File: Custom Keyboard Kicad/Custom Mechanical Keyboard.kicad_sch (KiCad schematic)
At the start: 288 parts, among them J1 USB_C_Receptacle_USB2.0_16P, J2 Conn_01x04, J3 Conn_01x05, J4 Conn_01x06, J5 Conn_01x07, J6 Conn_01x20_Socket, J7 Conn_01x20_Socket, SW1 SW_SPST, SW10 SW_SPST, SW11 SW_SPST, SW12 SW_SPST, SW13 SW_SPST, SW14 SW_SPST, SW15 SW_SPST, SW16 SW_SPST, SW17 SW_SPST, SW18 SW_SPST, SW19 SW_SPST, SW2 SW_SPST, SW20 SW_SPST, SW21 SW_SPST, SW22 SW_SPST, SW23 SW_SPST, SW24 SW_SPST, SW25 SW_SPST, SW26 SW_SPST, SW27 SW_SPST, SW28 SW_SPST, SW29 SW_SPST, SW3 SW_SPST, SW30 SW_SPST, SW31 SW_SPST, SW32 SW_SPST, SW33 SW_SPST, SW34 SW_SPST, SW35 SW_SPST, SW36 SW_SPST, SW37 SW_SPST, SW38 SW_SPST, SW39 SW_SPST, SW4 SW_SPST, SW40 SW_SPST, SW41 SW_SPST, SW42 SW_SPST, SW43 SW_SPST, SW44 SW_SPST, SW45 SW_SPST, SW46 SW_SPST, SW47 SW_SPST, SW48 SW_SPST, SW49 SW_SPST, SW5 SW_SPST, SW50 SW_SPST, SW51 SW_SPST, SW52 SW_SPST, SW53 SW_SPST, SW54 SW_SPST, SW55 SW_SPST, SW56 SW_SPST, SW57 SW_SPST, SW58 SW_SPST, SW59 SW_SPST, SW6 SW_SPST, SW60 SW_SPST, SW61 SW_SPST, SW62 SW_SPST, SW63 SW_SPST, SW64 SW_SPST, SW65 SW_SPST, SW66 SW_SPST, SW67 SW_SPST, SW68 SW_SPST, SW69 SW_SPST, SW7 SW_SPST, SW70 SW_SPST, SW71 SW_SPST, SW72 SW_SPST, SW73 SW_SPST, SW74 SW_SPST, SW75 SW_SPST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

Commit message: Commit after exports
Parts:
- J6, J7: MFG Part # (none) -> FPC-05F-20PH20; Manufacturer (none) -> Xunpu; Type (none) -> SMD
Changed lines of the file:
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@@
 			)
 		)
+		(property "MFG Part #" "FPC-05F-20PH20"
+			(at 488.95 92.71 0)
+			(effects
+				(font
+					(size 1.27 1.27)
+				)
+				(hide yes)
+			)
+		)
+		(property "Manufacturer" "Xunpu"
+			(at 488.95 92.71 0)
+			(effects
+				(font
+					(size 1.27 1.27)
+				)
+				(hide yes)
+			)
+		)
+		(property "Type" "SMD"
+			(at 488.95 92.71 0)
+			(effects
+				(font
+					(size 1.27 1.27)
+				)
+				(hide yes)
+			)
+		)
 		(pin "7"
 		)
@@
 			(at 509.27 92.71 0)
 			(effects
+				(font
+					(size 1.27 1.27)
+				)
+				(hide yes)
+			)
+		)
+		(property "MFG Part #" "FPC-05F-20PH20"
+			(at 509.27 92.71 0)
+			(effects
+				(font
+					(size 1.27 1.27)
+				)
+				(hide yes)
+			)
+		)
+		(property "Manufacturer" "Xunpu"
+			(at 509.27 92.71 0)
+			(effects
+				(font
+					(size 1.27 1.27)
+				)
+				(hide yes)
+			)
+		)
+		(property "Type" "SMD"
+			(at 509.27 92.71 0)
+			(effects

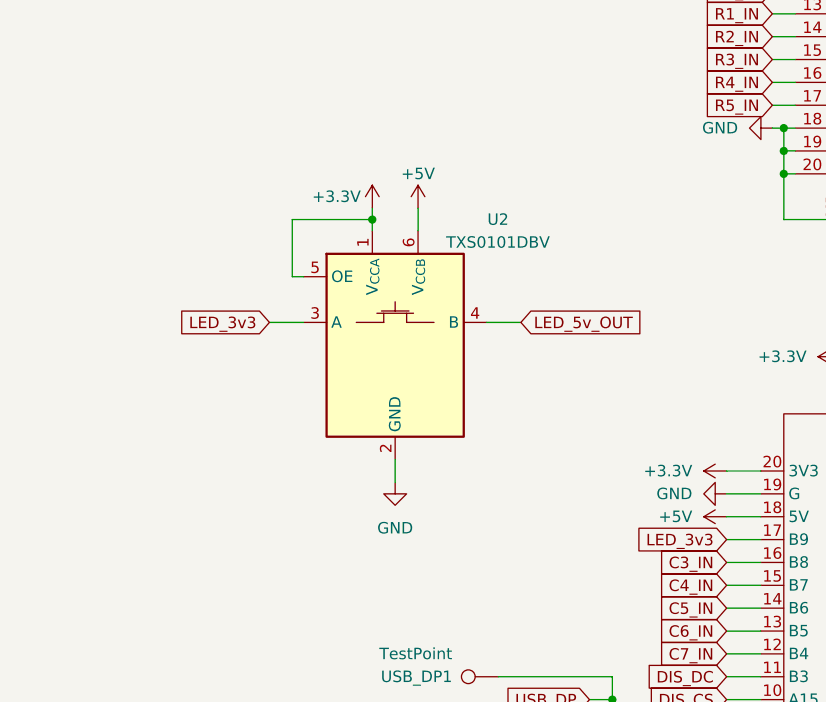
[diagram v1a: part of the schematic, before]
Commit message: Feat: Changed level shifter from TXS0101DBV to SN74LVC1T45DBV, footprint and wiring not changed.
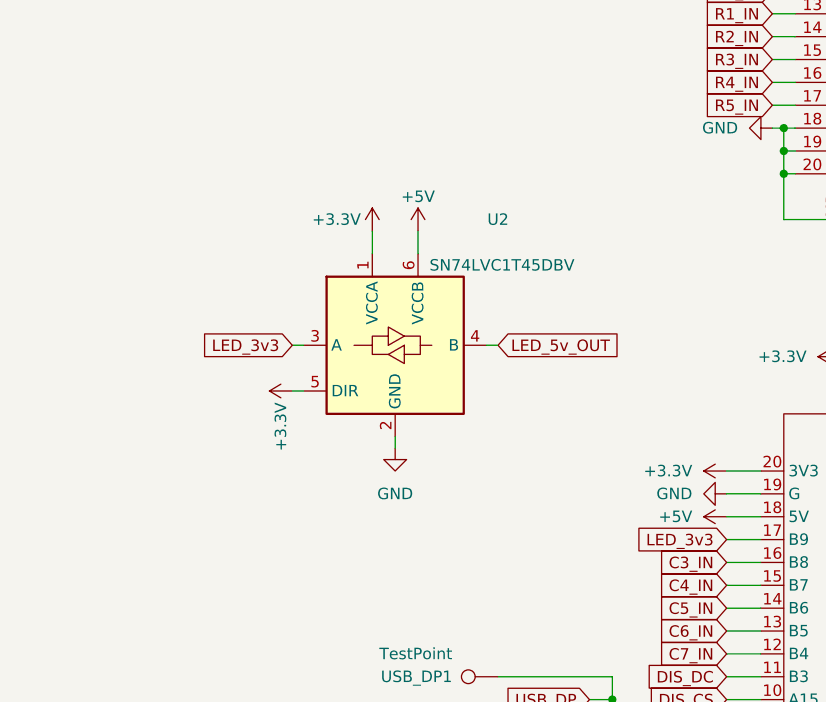
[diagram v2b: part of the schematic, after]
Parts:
- U2: value TXS0101DBV -> SN74LVC1T45DBV; symbol Logic_LevelTranslator:TXS0101DBV -> Logic_LevelTranslator:SN74LVC1T45DBV; MFG Part # TXS0101DBV -> SN74LVC1T45DBV\
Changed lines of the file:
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@@
 	)
 	(junction
-		(at 436.88 123.19)
-		(diameter 0)
-		(color 0 0 0 0)
-	)
-	(junction
 		(at 266.7 99.06)
 		(diameter 0)
@@
 	(wire
 		(pts
-			(xy 436.88 121.92) (xy 436.88 123.19)
-		)
-		(stroke
-			(width 0)
-			(type default)
-		)
-	)
-	(wire
-		(pts
 			(xy 374.65 332.74) (xy 374.65 330.2)
 		)
@@
 	(wire
 		(pts
-			(xy 441.96 121.92) (xy 441.96 124.46)
+			(xy 441.96 124.46) (xy 441.96 127)
 		)
 		(stroke
@@
 	(wire
 		(pts
-			(xy 144.78 54.61) (xy 144.78 55.88)
+			(xy 436.88 124.46) (xy 436.88 127)
 		)
 		(stroke
@@
 	(wire
 		(pts
-			(xy 63.5 142.24) (xy 83.82 142.24)
+			(xy 144.78 54.61) (xy 144.78 55.88)
 		)
 		(stroke
@@
 	(wire
 		(pts
-			(xy 340.36 36.83) (xy 340.36 45.72)
+			(xy 63.5 142.24) (xy 83.82 142.24)
 		)
 		(stroke
@@
 	(wire
 		(pts
-			(xy 320.04 67.31) (xy 318.77 67.31)
+			(xy 340.36 36.83) (xy 340.36 45.72)
 		)
 		(stroke
@@
 	(wire
 		(pts
-			(xy 171.45 210.82) (xy 191.77 210.82)
+			(xy 320.04 67.31) (xy 318.77 67.31)
 		)
 		(stroke
@@
 	(wire
 		(pts
-			(xy 427.99 123.19) (xy 436.88 123.19)
+			(xy 171.45 210.82) (xy 191.77 210.82)
 		)
 		(stroke
@@
 	(wire
 		(pts
-			(xy 425.45 134.62) (xy 429.26 134.62)
+			(xy 427.99 137.16) (xy 429.26 137.16)
 		)
 		(stroke
@@
 	(wire
 		(pts
-			(xy 427.99 129.54) (xy 427.99 123.19)
-		)
-		(stroke
-			(width 0)
-			(type default)
-		)
-	)
-	(wire
-		(pts
 			(xy 246.38 77.47) (xy 266.7 77.47)
 		)
@@
 	(wire
 		(pts
+			(xy 427.99 142.24) (xy 429.26 142.24)
+		)
+		(stroke
+			(width 0)
+			(type default)
+		)
+	)
+	(wire
+		(pts
 			(xy 165.1 133.35) (xy 165.1 132.08)
 		)
@@
 	(wire
 		(pts
-			(xy 436.88 123.19) (xy 436.88 124.46)
-		)
-		(stroke
-			(width 0)
-			(type default)
-		)
-	)
-	(wire
-		(pts
 			(xy 391.16 185.42) (xy 391.16 191.77)
 		)
@@
 	(wire
 		(pts
-			(xy 453.39 134.62) (xy 449.58 134.62)
+			(xy 450.85 137.16) (xy 449.58 137.16)
 		)
 		(stroke
@@
 	(wire
 		(pts
-			(xy 439.42 149.86) (xy 439.42 152.4)
+			(xy 439.42 147.32) (xy 439.42 148.59)
 		)
 		(stroke
@@
 	(wire
 		(pts
-			(xy 427.99 129.54) (xy 429.26 129.54)
-		)
-		(stroke
-			(width 0)
-			(type default)
-		)
-	)
-	(wire
-		(pts
 			(xy 405.13 199.39) (xy 405.13 205.74)
 		)
@@
 	(global_label "LED_3v3"
 		(shape input)
-		(at 425.45 134.62 180)
+		(at 427.99 137.16 180)
 		(fields_autoplaced yes)
 		(effects
@@
 		)
 		(property "Intersheetrefs" "${INTERSHEET_REFS}"
-			(at 414.6635 134.62 0)
+			(at 417.2035 137.16 0)
 			(effects
 				(font
@@
 	(global_label "LED_5v_OUT"
 		(shape input)
-		(at 453.39 134.62 0)
+		(at 450.85 137.16 0)
 		(fields_autoplaced yes)
 		(effects
@@
 		)
 		(property "Intersheetrefs" "${INTERSHEET_REFS}"
-			(at 467.5632 134.62 0)
+			(at 465.0232 137.16 0)
 			(effects
 				(font
@@
 	(symbol
 		(lib_id "power:+3.3V")
-		(at 436.88 121.92 0)
+		(at 436.88 124.46 0)
 		(unit 1)
 		(exclude_from_sim no)
@@
 		(dnp no)
 		(property "Reference" "#PWR013"
-			(at 436.88 125.73 0)
+			(at 436.88 128.27 0)
 			(effects
 				(font
@@
 		)
 		(property "Value" "+3.3V"
-			(at 435.61 120.65 0)
+			(at 435.61 123.19 0)
 			(effects
 				(font
@@
 		)
 		(property "Footprint" ""
-			(at 436.88 121.92 0)
+			(at 436.88 124.46 0)
 			(effects
 				(font
@@
 		)
 		(property "Datasheet" ""
-			(at 436.88 121.92 0)
+			(at 436.88 124.46 0)
 			(effects
 				(font
@@
 		)
 		(property "Description" "Power symbol creates a global label with name \"+3.3V\""
-			(at 436.88 121.92 0)
+			(at 436.88 124.46 0)
 			(effects
 				(font
@@
 	)
 	(symbol
-		(lib_id "Logic_LevelTranslator:TXS0101DBV")
+		(lib_id "Logic_LevelTranslator:SN74LVC1T45DBV")
 		(at 439.42 137.16 0)
 		(unit 1)
@@
 			)
 		)
-		(property "Value" "TXS0101DBV"
-			(at 450.85 125.73 0)
+		(property "Value" "SN74LVC1T45DBV"
+			(at 443.23 128.27 0)
 			(effects
 				(font
 					(size 1.27 1.27)
 				)
+				(justify left)
 			)
 		)
 		(property "Footprint" "Package_TO_SOT_SMD:SOT-23-6"
-			(at 440.69 148.59 0)
+			(at 439.42 148.59 0)
 			(effects
 				(font
 					(size 1.27 1.27)
 				)
-				(justify left)
 				(hide yes)
 			)
 		)
-		(property "Datasheet" "https://www.ti.com/lit/ds/symlink/txs0101.pdf"
-			(at 439.42 161.29 0)
+		(property "Datasheet" "http://www.ti.com/lit/ds/symlink/sn74lvc1t45.pdf"
+			(at 416.56 153.67 0)
 			(effects
 				(font
@@
 			)
 		)
-		(property "Description" "1-Bit Bidirectional Voltage-Level Shifter for Open-Drain and Push-Pull Application, SOT-23"
+		(property "Description" "Single-Bit Dual-Supply Bus Transceiver With Configurable Voltage Translation and 3-State Outputs, SOT-23-6"
 			(at 439.42 137.16 0)
 			(effects
@@
 			)
 		)
-		(property "MFG Part #" "TXS0101DBV"
+		(property "MFG Part #" "SN74LVC1T45DBV\\"
 			(at 439.42 137.16 0)
 			(effects
@@
 	(symbol
 		(lib_id "power:GND")
-		(at 439.42 152.4 0)
+		(at 439.42 148.59 0)
 		(unit 1)
 		(exclude_from_sim no)
@@
 		(fields_autoplaced yes)
 		(property "Reference" "#PWR019"
-			(at 439.42 158.75 0)
+			(at 439.42 154.94 0)
 			(effects
 				(font
@@
 		)
 		(property "Value" "GND"
-			(at 439.42 157.48 0)
+			(at 439.42 153.67 0)
 			(effects
 				(font
@@
 		)
 		(property "Footprint" ""
-			(at 439.42 152.4 0)
+			(at 439.42 148.59 0)
 			(effects
 				(font
@@
 		)
 		(property "Datasheet" ""
-			(at 439.42 152.4 0)
+			(at 439.42 148.59 0)
 			(effects
 				(font
@@
 		)
 		(property "Description" "Power symbol creates a global label with name \"GND\" , ground"
-			(at 439.42 152.4 0)
+			(at 439.42 148.59 0)
 			(effects
 				(font
@@
 	(symbol
 		(lib_id "power:+5V")
-		(at 441.96 121.92 0)
+		(at 441.96 124.46 0)
 		(unit 1)
 		(exclude_from_sim no)
@@
 		(dnp no)
 		(property "Reference" "#PWR014"
-			(at 441.96 125.73 0)
+			(at 441.96 128.27 0)
 			(effects
 				(font
@@
 		)
 		(property "Value" "+5V"
-			(at 441.96 118.11 0)
+			(at 441.96 120.65 0)
 			(effects
 				(font
@@
 		)
 		(property "Footprint" ""
-			(at 441.96 121.92 0)
+			(at 441.96 124.46 0)
 			(effects
 				(font
@@
 		)
 		(property "Datasheet" ""
-			(at 441.96 121.92 0)
+			(at 441.96 124.46 0)
 			(effects
 				(font
@@
 		)
 		(property "Description" "Power symbol creates a global label with name \"+5V\""
-			(at 441.96 121.92 0)
+			(at 441.96 124.46 0)
 			(effects
 				(font
@@
 					(unit 1)
 				)
+			)
+		)
+	)
+	(symbol
+		(lib_id "power:+3.3V")
+		(at 427.99 142.24 90)
+		(unit 1)
+		(exclude_from_sim no)
+		(in_bom yes)
+		(on_board yes)
+		(dnp no)
+		(property "Reference" "#PWR043"
+			(at 431.8 142.24 0)
+			(effects
+				(font
+					(size 1.27 1.27)
+				)
+				(hide yes)
+			)
+		)
+		(property "Value" "+3.3V"
+			(at 426.72 143.51 0)
+			(effects
+				(font
+					(size 1.27 1.27)
+				)
+				(justify right)
+			)
+		)
+		(property "Footprint" ""
+			(at 427.99 142.24 0)
+			(effects
+				(font
+					(size 1.27 1.27)
+				)
+				(hide yes)
+			)
+		)
+		(property "Datasheet" ""
+			(at 427.99 142.24 0)
+			(effects
+				(font
+					(size 1.27 1.27)
+				)
+				(hide yes)
+			)
+		)
+		(property "Description" "Power symbol creates a global label with name \"+3.3V\""
+			(at 427.99 142.24 0)
+			(effects
+				(font
+					(size 1.27 1.27)
+				)
+				(hide yes)
+			)
+		)
+		(pin "1"
+		)
+		(instances
+			(project "Custom Mechanical Keyboard"
+				(path "/bf85d36b-b543-4af2-8831-9827a94ddedd"
+					(reference "#PWR043")
+					(unit 1)
+				)

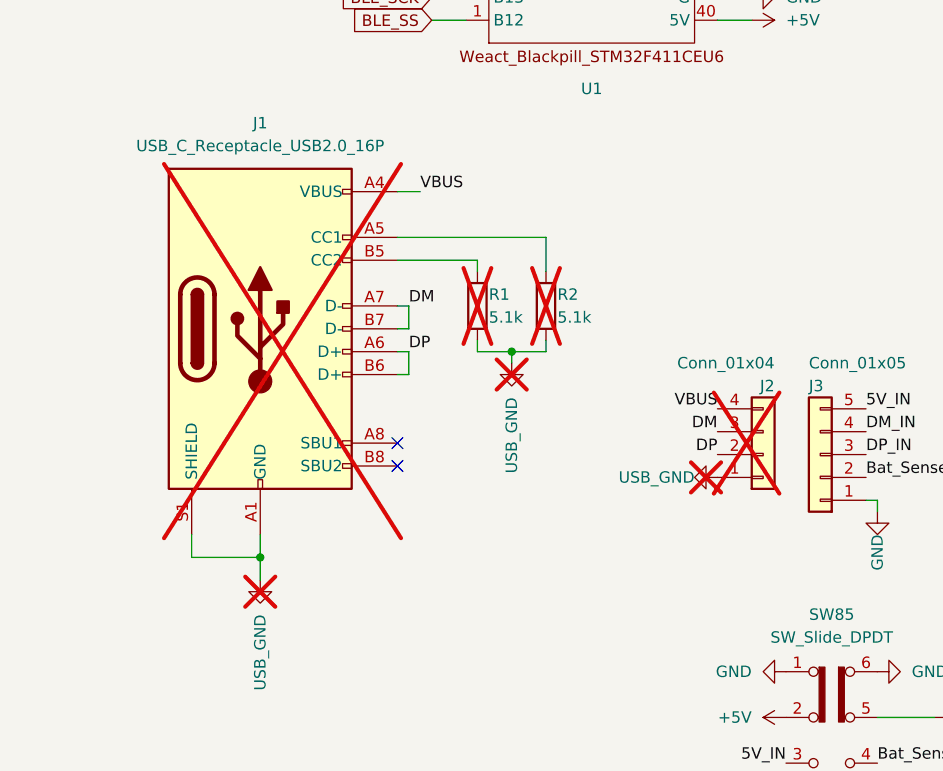
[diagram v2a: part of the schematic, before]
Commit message: Feat: Added USB PCB, edited PCM Master Lib sunken usb-c port - changed pcb edge line to drawing to allow for edge cut line connection
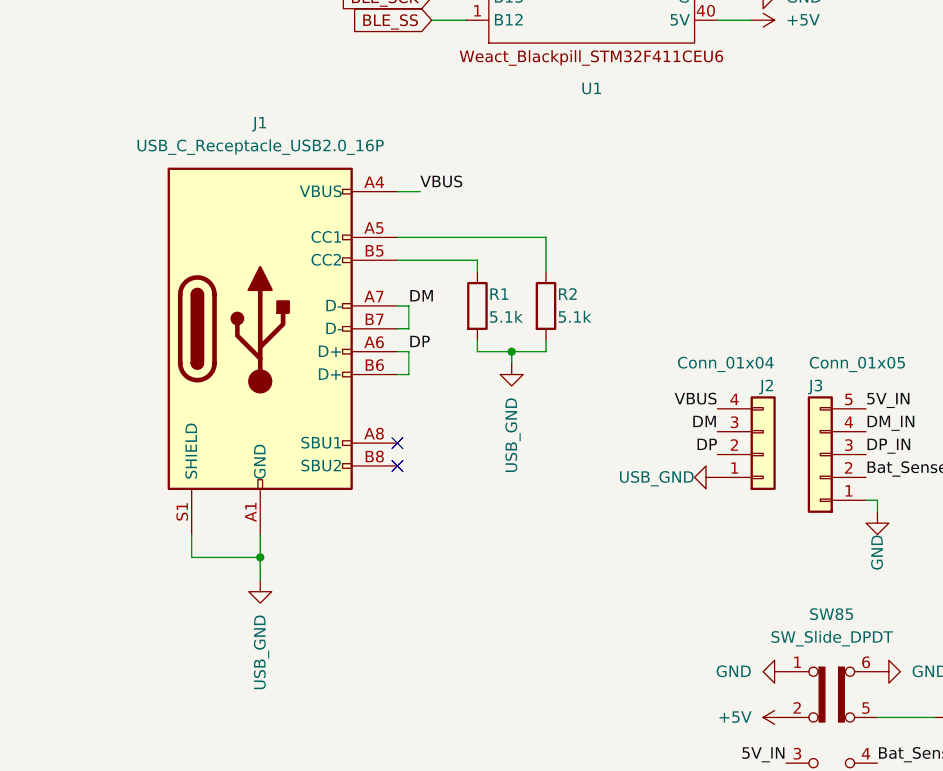
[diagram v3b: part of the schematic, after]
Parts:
- J1, J2, R1, R2: now fitted; now in the parts list
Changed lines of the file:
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@@
 		(unit 1)
 		(exclude_from_sim no)
-		(in_bom no)
-		(on_board no)
-		(dnp yes)
+		(in_bom yes)
+		(on_board yes)
+		(dnp no)
 		(property "Reference" "#PWR017"
 			(at 485.14 243.84 0)
@@
 		(unit 1)
 		(exclude_from_sim no)
-		(in_bom no)
-		(on_board no)
-		(dnp yes)
+		(in_bom yes)
+		(on_board yes)
+		(dnp no)
 		(property "Reference" "J2"
 			(at 514.35 240.03 0)
@@
 		(unit 1)
 		(exclude_from_sim no)
-		(in_bom no)
-		(on_board no)
-		(dnp yes)
+		(in_bom yes)
+		(on_board yes)
+		(dnp no)
 		(property "Reference" "R2"
 			(at 490.22 229.87 0)
@@
 		(unit 1)
 		(exclude_from_sim no)
-		(in_bom no)
-		(on_board no)
-		(dnp yes)
+		(in_bom yes)
+		(on_board yes)
+		(dnp no)
 		(property "Reference" "J1"
 			(at 457.2 210.82 0)
@@
 		(unit 1)
 		(exclude_from_sim no)
-		(in_bom no)
-		(on_board no)
-		(dnp yes)
+		(in_bom yes)
+		(on_board yes)
+		(dnp no)
 		(property "Reference" "R1"
 			(at 482.6 229.87 0)
@@
 		(unit 1)
 		(exclude_from_sim no)
-		(in_bom no)
-		(on_board no)
-		(dnp yes)
+		(in_bom yes)
+		(on_board yes)
+		(dnp no)
 		(property "Reference" "#PWR028"
 			(at 501.65 250.19 0)
@@
 		(unit 1)
 		(exclude_from_sim no)
-		(in_bom no)
-		(on_board no)
-		(dnp yes)
+		(in_bom yes)
+		(on_board yes)
+		(dnp no)
 		(property "Reference" "#PWR021"
 			(at 457.2 267.97 0)

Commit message: Fix: Changed USB C receptacle to 31M12 instead of 31M14 to fit cheaper assembly requirements
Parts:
- J1: footprint PCM_marbastlib-various:USB_C_Receptacle_HRO_TYPE-C-31-M-14_(polygon_edge) -> PCM_marbastlib-various:USB_C_Receptacle_HRO_TYPE-C-31-M-12; MFG Part # (none) -> TYPE-C-31-M-14; Manufacturer (none) -> Korean Hroparts; Type (none) -> Thru-Hole
- J2: now left out of the parts list
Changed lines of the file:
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@@
 		(unit 1)
 		(exclude_from_sim no)
-		(in_bom yes)
+		(in_bom no)
 		(on_board yes)
 		(dnp no)
@@
 			)
 		)
-		(property "Footprint" "PCM_marbastlib-various:USB_C_Receptacle_HRO_TYPE-C-31-M-14_(polygon_edge)"
+		(property "Footprint" "PCM_marbastlib-various:USB_C_Receptacle_HRO_TYPE-C-31-M-12"
 			(at 461.01 233.68 0)
 			(effects
@@
 			)
 		)
-		(property "MFG Part #" ""
+		(property "MFG Part #" "TYPE-C-31-M-14"
 			(at 457.2 233.68 0)
 			(effects
@@
 			)
 		)
-		(property "Manufacturer" ""
+		(property "Manufacturer" "Korean Hroparts"
 			(at 457.2 233.68 0)
 			(effects
@@
 			)
 		)
-		(property "Type" ""
+		(property "Type" "Thru-Hole"
 			(at 457.2 233.68 0)
 			(effects
